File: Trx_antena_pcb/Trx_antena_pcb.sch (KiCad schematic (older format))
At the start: 3 parts

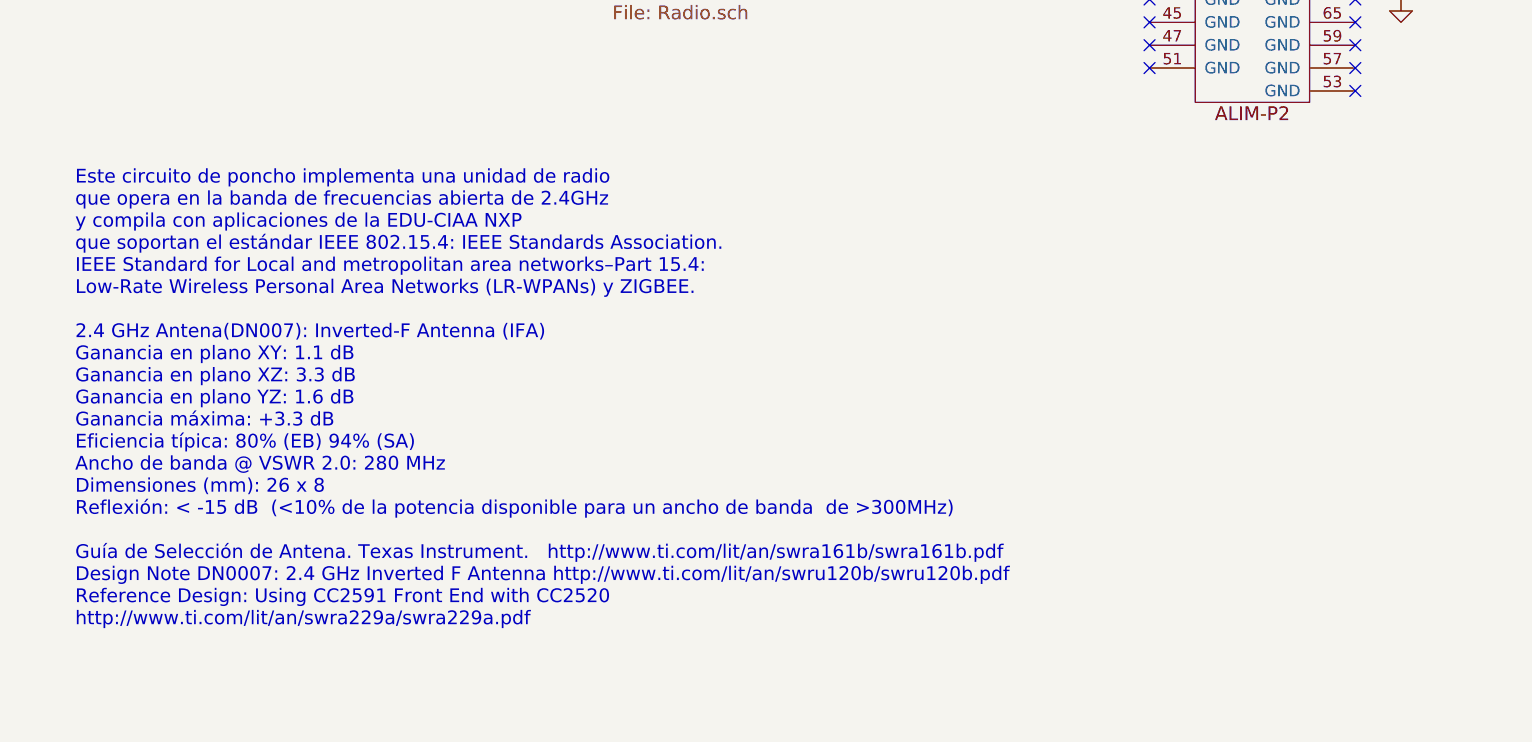
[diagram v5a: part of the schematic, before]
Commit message: layout de componentes en pcbnew
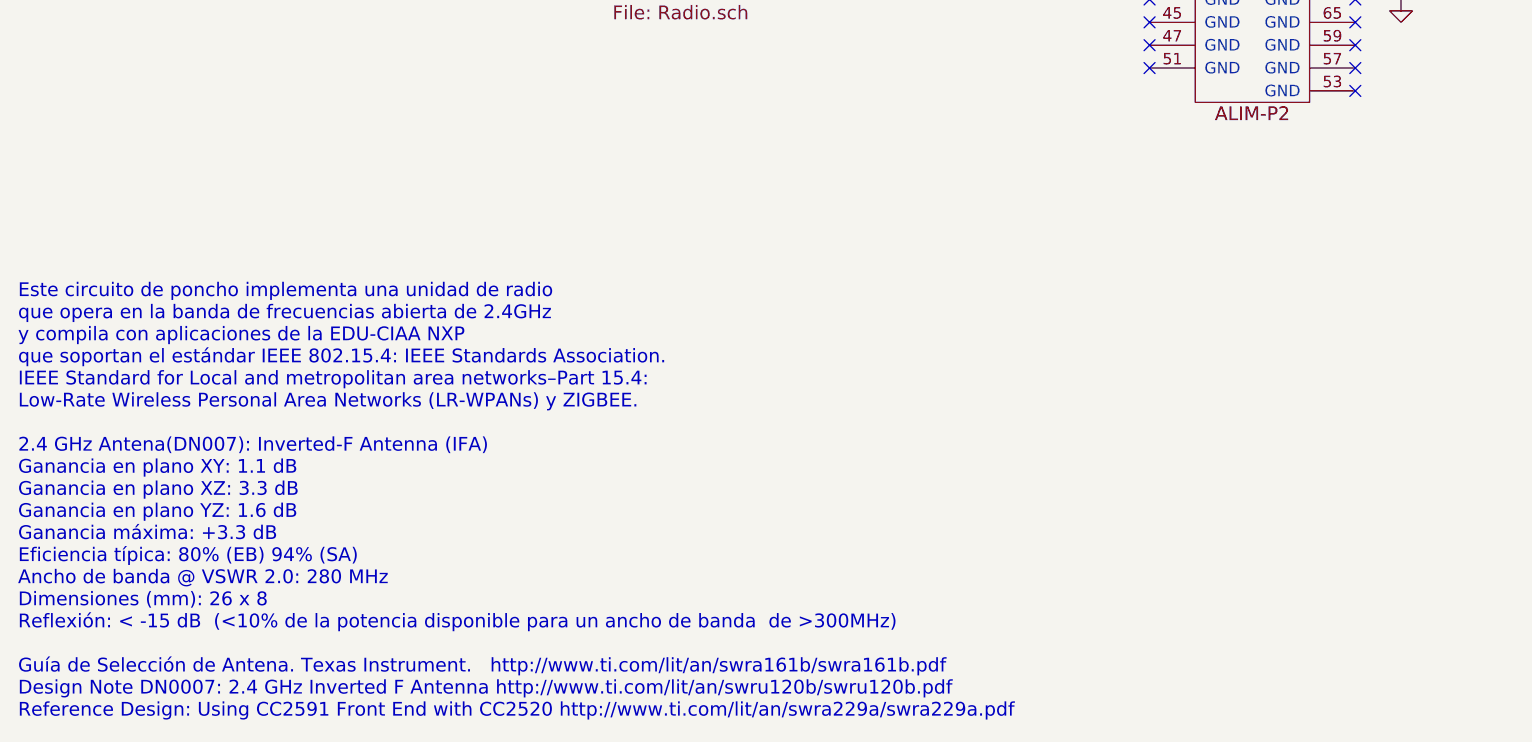
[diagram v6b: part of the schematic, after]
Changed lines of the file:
@@
 Wire Wire Line
 	4300 2200 4150 2200
-Text Notes 1000 7200 0    60   ~ 0
-Este circuito de poncho implementa una unidad de radio \nque opera en la banda de frecuencias abierta de 2.4GHz \ny compila con aplicaciones de la EDU-CIAA NXP \nque soportan el estándar IEEE 802.15.4: IEEE Standards Association. \nIEEE Standard for Local and metropolitan area networks–Part 15.4: \nLow-Rate Wireless Personal Area Networks (LR-WPANs) y ZIGBEE.\n\n2.4 GHz Antena(DN007): Inverted-F Antenna (IFA) \nGanancia en plano XY: 1.1 dB\nGanancia en plano XZ: 3.3 dB\nGanancia en plano YZ: 1.6 dB\nGanancia máxima: +3.3 dB\nEficiencia típica: 80% (EB) 94% (SA)\nAncho de banda @ VSWR 2.0: 280 MHz\nDimensiones (mm): 26 x 8\nReflexión: < -15 dB  (<10% de la potencia disponible para un ancho de banda  de >300MHz)\n\nGuía de Selección de Antena. Texas Instrument.   http://www.ti.com/lit/an/swra161b/swra161b.pdf\nDesign Note DN0007: 2.4 GHz Inverted F Antenna http://www.ti.com/lit/an/swru120b/swru120b.pdf\nReference Design: Using CC2591 Front End with CC2520\nhttp://www.ti.com/lit/an/swra229a/swra229a.pdf
+Text Notes 750  7600 0    60   ~ 0
+Este circuito de poncho implementa una unidad de radio \nque opera en la banda de frecuencias abierta de 2.4GHz \ny compila con aplicaciones de la EDU-CIAA NXP \nque soportan el estándar IEEE 802.15.4: IEEE Standards Association. \nIEEE Standard for Local and metropolitan area networks–Part 15.4: \nLow-Rate Wireless Personal Area Networks (LR-WPANs) y ZIGBEE.\n\n2.4 GHz Antena(DN007): Inverted-F Antenna (IFA) \nGanancia en plano XY: 1.1 dB\nGanancia en plano XZ: 3.3 dB\nGanancia en plano YZ: 1.6 dB\nGanancia máxima: +3.3 dB\nEficiencia típica: 80% (EB) 94% (SA)\nAncho de banda @ VSWR 2.0: 280 MHz\nDimensiones (mm): 26 x 8\nReflexión: < -15 dB  (<10% de la potencia disponible para un ancho de banda  de >300MHz)\n\nGuía de Selección de Antena. Texas Instrument.   http://www.ti.com/lit/an/swra161b/swra161b.pdf\nDesign Note DN0007: 2.4 GHz Inverted F Antenna http://www.ti.com/lit/an/swru120b/swru120b.pdf\nReference Design: Using CC2591 Front End with CC2520 http://www.ti.com/lit/an/swra229a/swra229a.pdf
 $EndSCHEMATC
